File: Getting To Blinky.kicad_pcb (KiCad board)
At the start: 2 copper layers, 35.6 x 27.9 mm, 6 parts, among them U1 7555

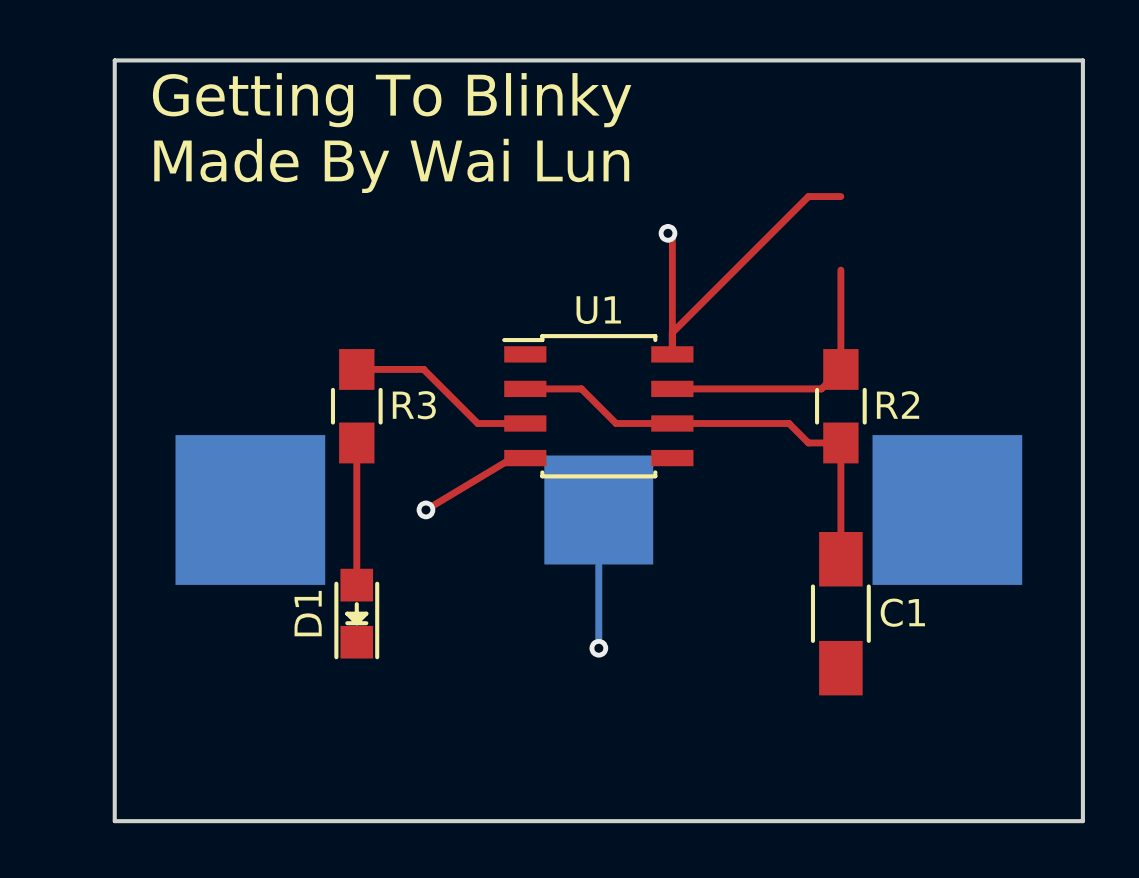
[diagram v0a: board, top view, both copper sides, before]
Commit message: Displaced 555 IC & Removed Battery Holder Pads
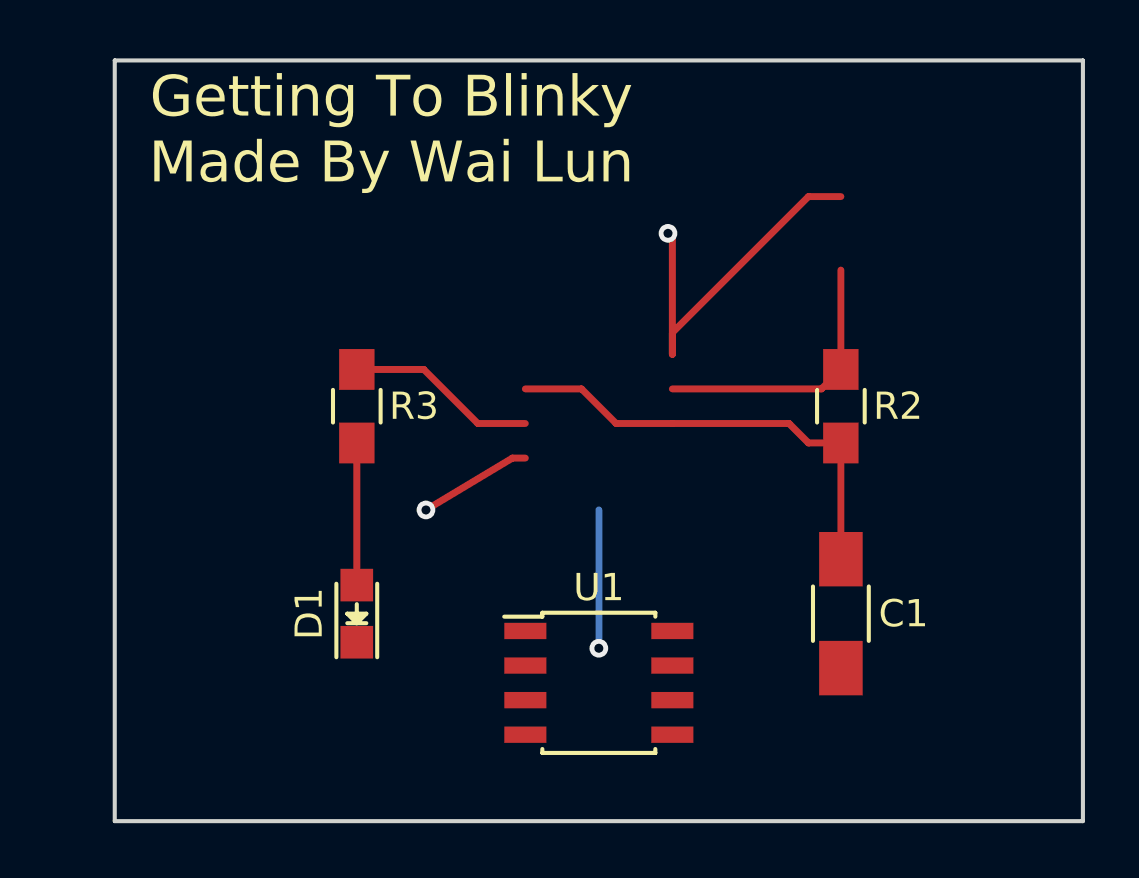
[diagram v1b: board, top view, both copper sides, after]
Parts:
- removed BT1: Battery, GTB:S8211R
- moved U1 10.2 mm to (139.7, 109.2)
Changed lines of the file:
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@@
     (tracks 25)
     (zones 0)
-    (modules 6)
+    (modules 5)
     (nets 7)
   )
@@
   )
   (module Housings_SOIC:SOIC-8_3.9x4.9mm_Pitch1.27mm (layer F.Cu)
-    (at 139.7 99.06)
+    (at 139.7 109.22)
     (descr "8-Lead Plastic Small Outline (SN) - Narrow, 3.90 mm Body [SOIC] (see Microchip Packaging Specification 00000049BS.pdf)")
     (tags "SOIC 1.27")
@@
     )
   )
-  (module GTB:S8211R (layer B.Cu)
-    (at 139.7 102.87)
-    (fp_text reference BT1 (at 11.43 10.16) (layer B.SilkS)
-      (effects (font (size 1 1) (thickness 0.15)) (justify mirror))
-    )
-    (fp_text value Battery (at -10.16 10.16) (layer B.Fab)
-      (effects (font (size 1 1) (thickness 0.15)) (justify mirror))
-    )
-    (fp_line (start 12.7 6.35) (end 12.7 -8.89) (layer B.SilkS) (width 0.15))
-    (fp_line (start 12.7 -8.89) (end 0 -15.24) (layer B.SilkS) (width 0.15))
-    (fp_line (start 0 -15.24) (end -12.7 -8.89) (layer B.SilkS) (width 0.15))
-    (fp_line (start -12.7 -8.89) (end -12.7 8.89) (layer B.SilkS) (width 0.15))
-    (fp_line (start -12.7 8.89) (end 12.7 8.89) (layer B.SilkS) (width 0.15))
-    (fp_line (start 12.7 8.89) (end 12.7 6.35) (layer B.SilkS) (width 0.15))
-    (pad 2 smd rect (at 0 0) (size 4 4) (layers B.Cu B.Paste B.Mask)
-      (net 2 GND))
-    (pad 1 smd rect (at -12.8 0) (size 5.5 5.5) (layers B.Cu B.Paste B.Mask)
-      (net 4 /VDD))
-    (pad 1 smd rect (at 12.8 0) (size 5.5 5.5) (layers B.Cu B.Paste B.Mask)
-      (net 4 /VDD))
-  )
   (gr_text "Getting To Blinky\nMade By Wai Lun" (at 132.08 88.9) (layer F.SilkS)
